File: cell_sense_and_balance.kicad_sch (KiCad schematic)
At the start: 40 parts, among them U1 BQ79616PAPRQ1

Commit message: SCH:[Hiarchy, Temp, Power]:Inital schmatics of temp, balance, power mostly there need to add design notes and layout notes.
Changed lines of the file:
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@@
-		)
-	)
-	(label "TAP[0..8]"
-		(at 116.84 53.34 0)
-		(fields_autoplaced yes)
-		(effects
-			(font
-				(size 1.27 1.27)
-			)
-			(justify left bottom)
-		)
-		(property "Netclass" "TAP"
-			(at 116.84 54.61 0)
-			(show_name no)
-			(do_not_autoplace no)
-			(effects
-				(font
-					(size 1.27 1.27)
-					(italic yes)
-				)
-				(justify left)
-			)
 		)
 	)
@@
 		)
 	)
-	(hierarchical_label "CELL_TAPS"
+	(hierarchical_label "TAP[0..8]"
 		(shape bidirectional)
 		(at 116.84 53.34 180)
@@
 			(justify right)
 		)
+		(property "Netclass" "TAP"
+			(at 106.68 55.88 0)
+			(show_name no)
+			(do_not_autoplace no)
+			(effects
+				(font
+					(size 1.27 1.27)
+					(italic yes)
+				)
+				(justify left)
+			)
+		)
 	)

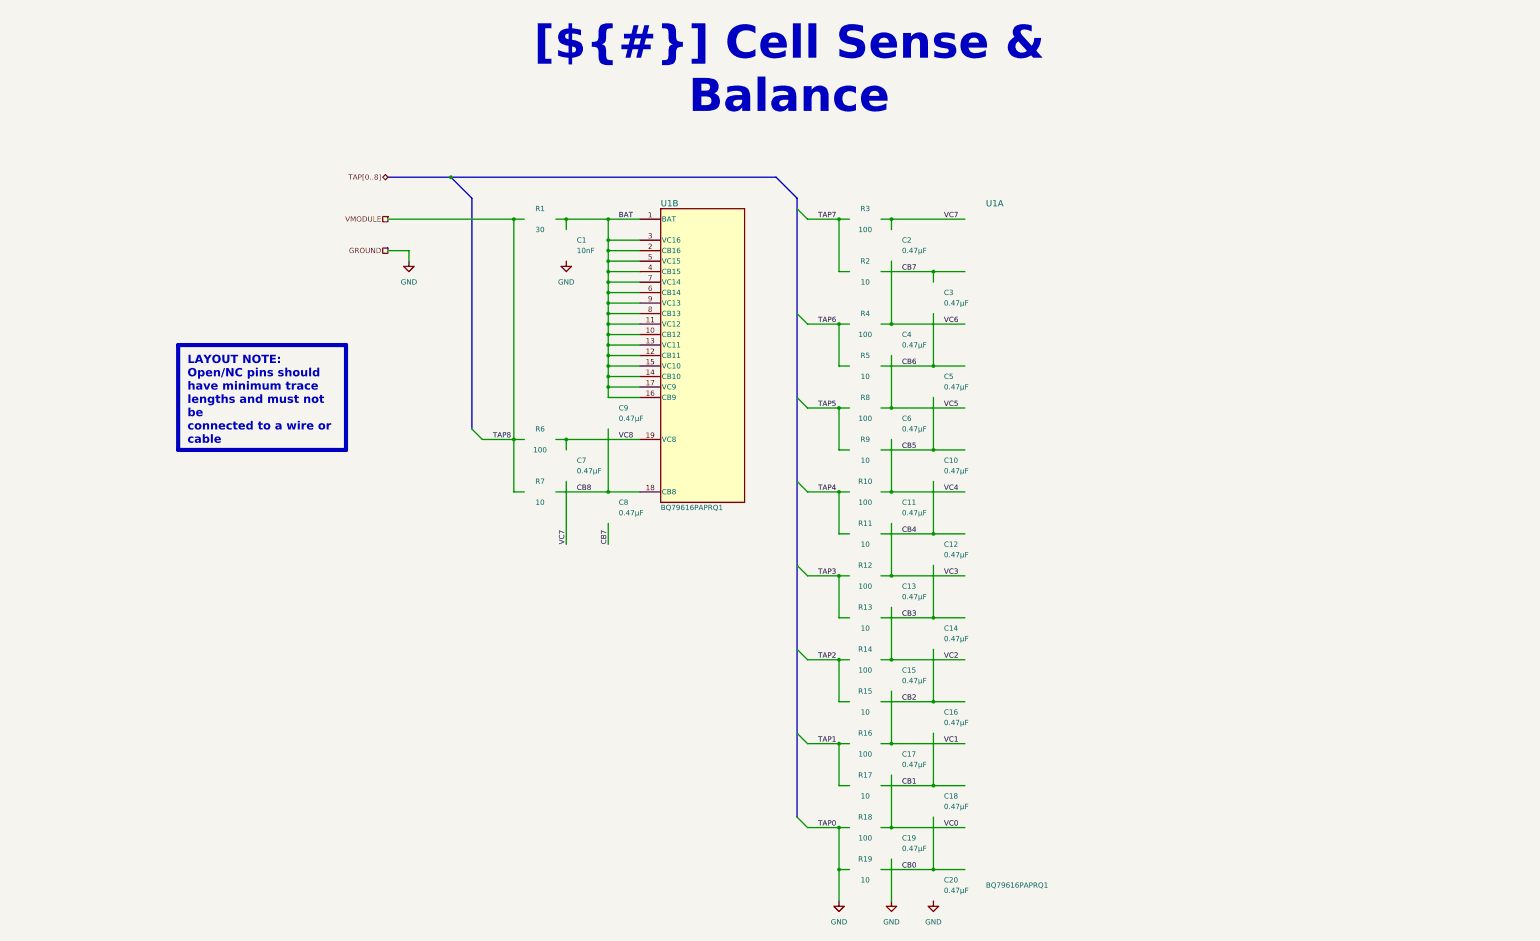
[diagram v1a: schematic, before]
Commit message: SCH: Schmatic is close to final, need to resolve a few ERC errors nothing major. Largest change will be adding seporate wires for VBAT and RefGround / Tap 0. connector position and types may change as mechaincal posision/layout is finalaized as well so holding off on layout for now.
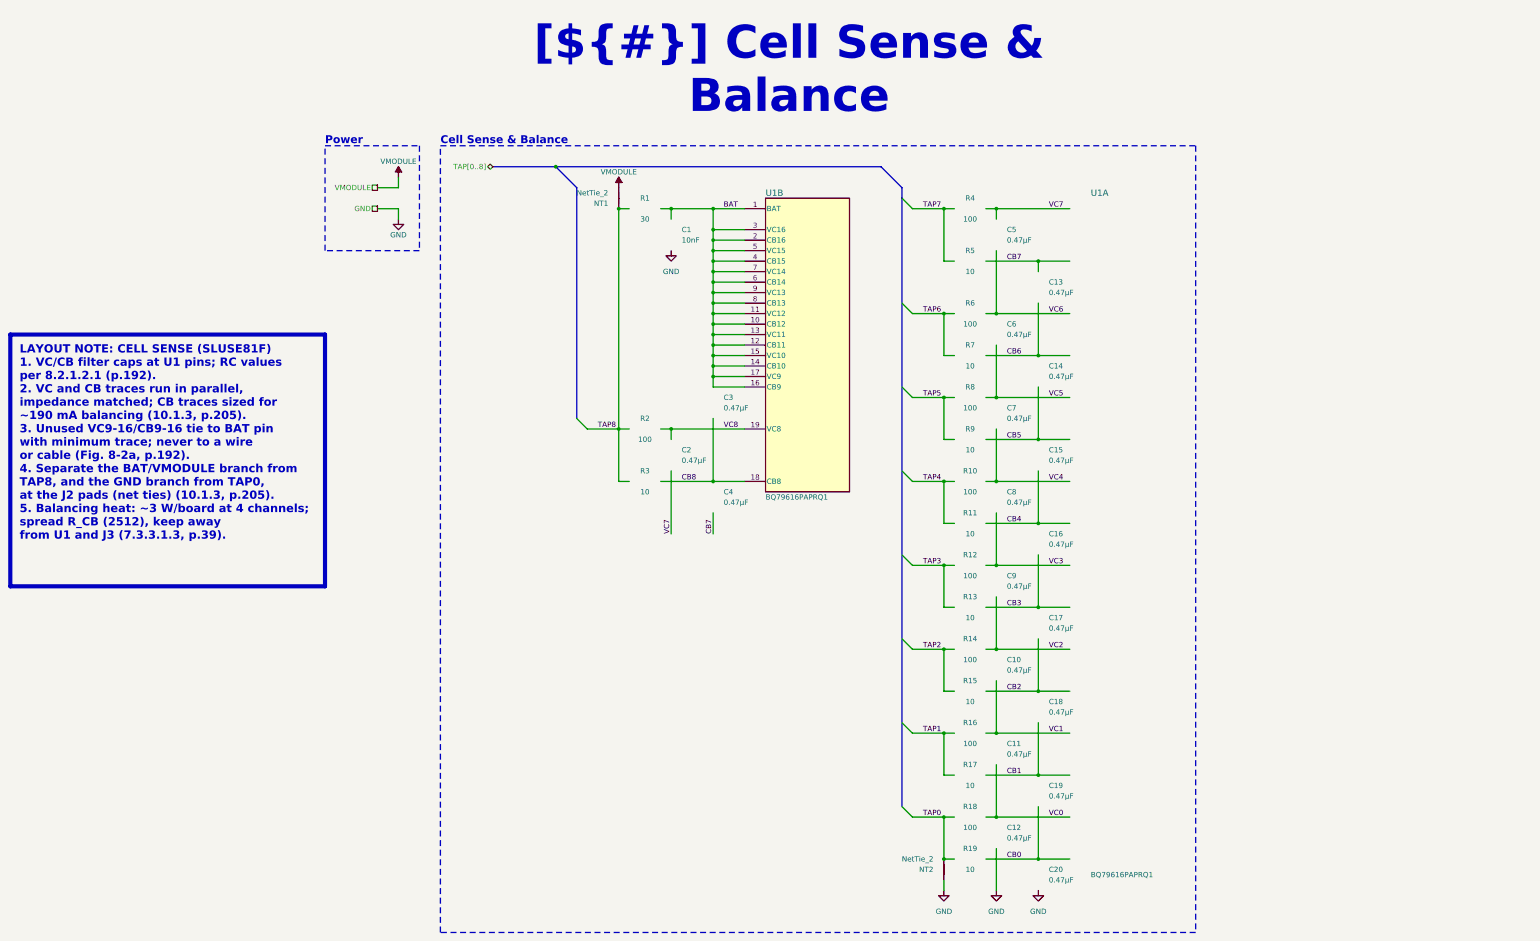
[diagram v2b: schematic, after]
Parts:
- added NT1, NT2: NetTie_2, symbol Device:NetTie_2
- renumbered C15 to C10, C17 to C11, C19 to C12, C3 to C13, C5 to C14, C10 to C15, C12 to C16, C14 to C17, C16 to C18, C18 to C19, C7 to C2, C9 to C3, C8 to C4, C2 to C5, C4 to C6, C6 to C7, C11 to C8, C13 to C9, R6 to R2, R7 to R3, R3 to R4, R2 to R5, R4 to R6, R5 to R7
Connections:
- net GND: now also NT2.1; no longer R18.1, R19.1
- net VMODULE: now also NT1.2; no longer R1.1, R2.1, R3.1
- new net TAP0: NT2.2, R18.1, R19.1
- new net TAP8: NT1.1, R1.1, R2.1, R3.1
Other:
- note added: "Cell Sense & Balance"
- note added: "Power"
- moved on the sheet: U1B

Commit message: SCH[Cleaning]:Updated Connectors not sure still, added sprate bat and ground connections, updated commincation conncetors. PCB[Layout]:Inital layout of compents need to fit on board size once tap connecton method is decided.
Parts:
- removed NT1, NT2: NetTie_2, symbol Device:NetTie_2
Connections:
- net TAP8: no longer R1.1
- net VMODULE: now also R1.1

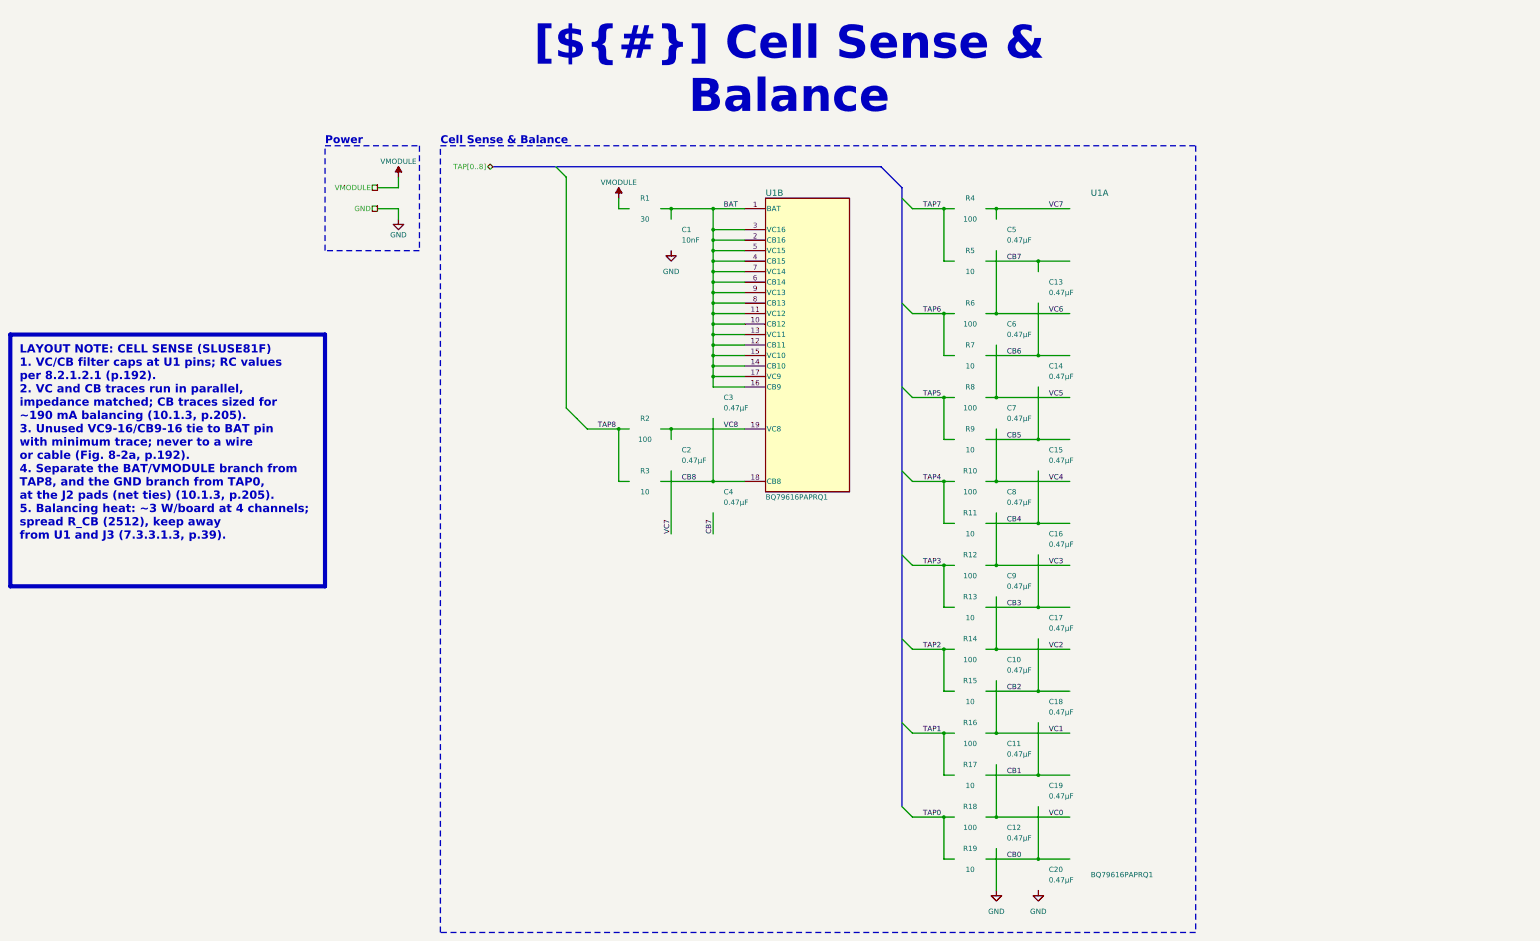
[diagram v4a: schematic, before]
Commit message: PCB[Test Points, Mechanical, Silk]: Finalized Mounting Points, Added Testpoints with adjecent silkscreen labels. SCH[Test Points, Notes]: Added/Updated notes for all pages, cleaned up errors spelling ect.
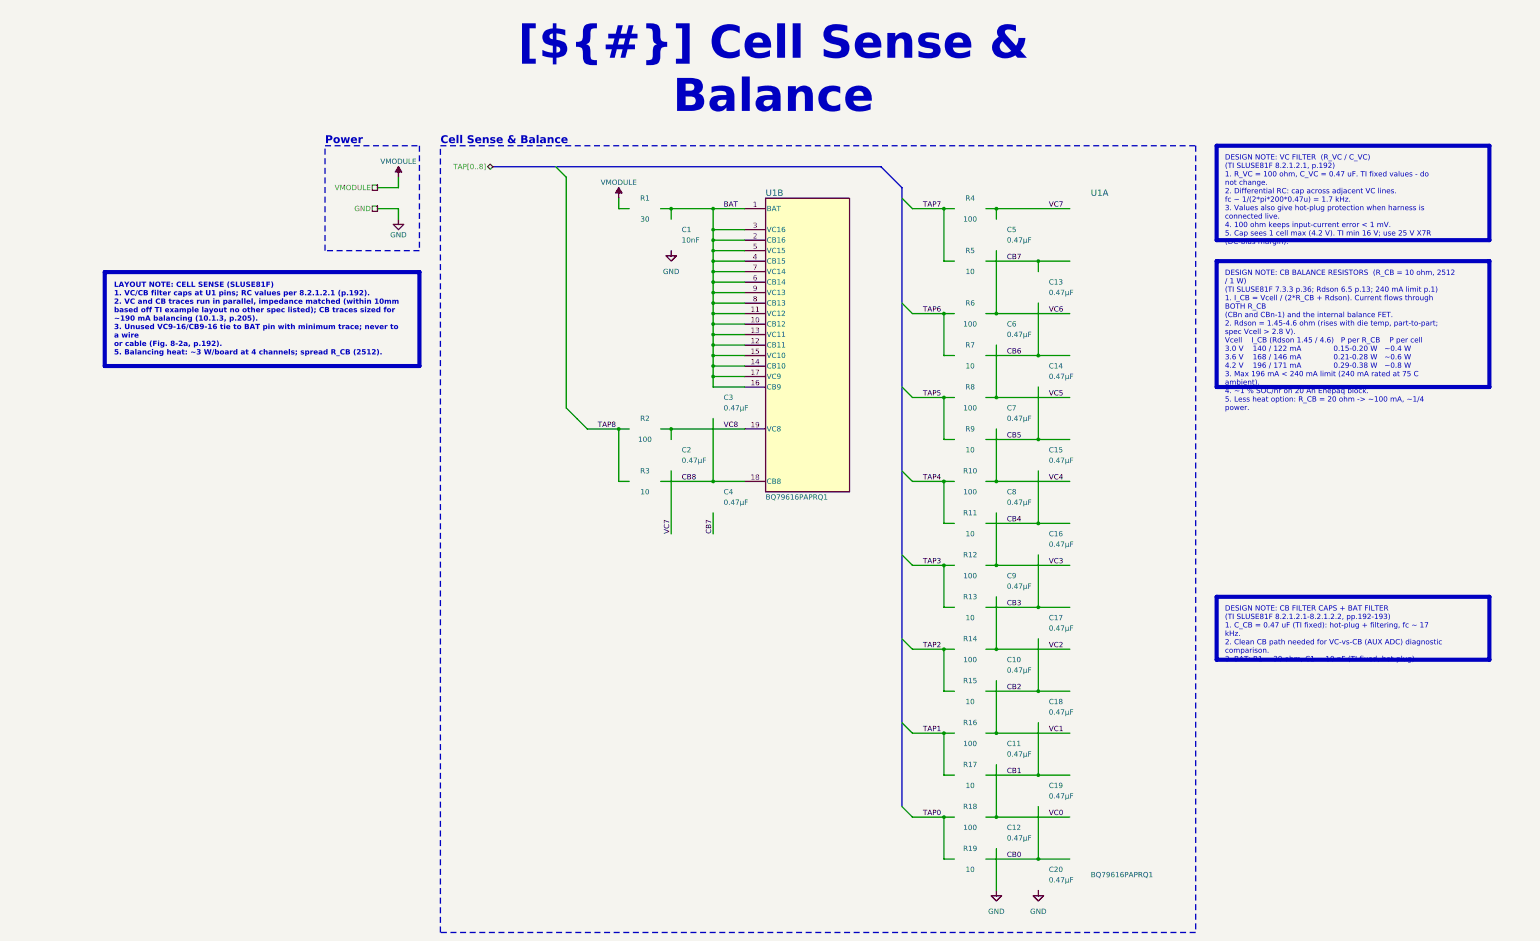
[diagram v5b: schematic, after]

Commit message: PCB[Trace Size, Testpad, Daisy]: Changed Bat Trace size FAT, Made test pads larger, small trace movement to clean up, daisy trace change. SCH[Notes]: Small notes changes.
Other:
- company: (none) -> ${COMPANY}
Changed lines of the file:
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@@
 	(title_block
 		(title "Cell Sense & Balance")
+		(date "2026-10-28")
+		(rev "${REVISION}")
+		(company "${COMPANY}")
 	)
 	(rectangle
@@
 		)
 	)
-	(text_box "DESIGN NOTE: VC FILTER  (R_VC / C_VC)\n(TI SLUSE81F 8.2.1.2.1, p.192)\n1. R_VC = 100 ohm, C_VC = 0.47 uF. TI fixed values - do not change.\n2. Differential RC: cap across adjacent VC lines.\n   fc ~ 1/(2*pi*200*0.47u) = 1.7 kHz.\n3. Values also give hot-plug protection when harness is connected live.\n4. 100 ohm keeps input-current error < 1 mV.\n5. Cap sees 1 cell max (4.2 V). TI min 16 V; use 25 V X7R (DC-bias margin)."
+	(text_box "DESIGN NOTE: VC FILTER  (R_VC / C_VC)\n(TI Datasheet 8.2.1.2.1, p.192)\n1. R_VC = 100 ohm, C_VC = 0.47 uF. TI fixed values, do not change.\n2. Differential RC: cap across adjacent VC lines.\n   fc ~ 1/(2*pi*200*0.47u) = 1.7 kHz.\n3. Values also give hot-plug protection when harness is connected live.\n4. 100 ohm keeps input-current error < 1 mV.\n5. Cap sees 1 cell max (4.2 V). TI min 16 V; use 25 V X7R (DC-bias margin)."
 		(exclude_from_sim no)
 		(at 317.5 45.72 0)
@@
 		)
 	)
-	(text_box "DESIGN NOTE: CB FILTER CAPS + BAT FILTER\n(TI SLUSE81F 8.2.1.2.1-8.2.1.2.2, pp.192-193)\n1. C_CB = 0.47 uF (TI fixed): hot-plug + filtering, fc ~ 17 kHz.\n2. Clean CB path needed for VC-vs-CB (AUX ADC) diagnostic comparison.\n3. BAT: R1 = 30 ohm, C1 = 10 nF (TI fixed, hot-plug)."
+	(text_box "DESIGN NOTE: CB FILTER CAPS + BAT FILTER\n(TI Datasheet 8.2.1.2.1-8.2.1.2.2, pp.192-193)\n1. C_CB = 0.47 uF (TI fixed): hot-plug + filtering, fc ~ 17 kHz.\n2. Clean CB path needed for VC-vs-CB (AUX ADC) diagnostic comparison.\n3. BAT: R1 = 30 ohm, C1 = 10 nF (TI fixed, hot-plug)."
 		(exclude_from_sim no)
 		(at 317.5 154.94 0)
@@
 		)
 	)
-	(text_box "DESIGN NOTE: CB BALANCE RESISTORS  (R_CB = 10 ohm, 2512 / 1 W)\n(TI SLUSE81F 7.3.3 p.36; Rdson 6.5 p.13; 240 mA limit p.1)\n1. I_CB = Vcell / (2*R_CB + Rdson). Current flows through BOTH R_CB\n   (CBn and CBn-1) and the internal balance FET.\n2. Rdson = 1.45-4.6 ohm (rises with die temp, part-to-part; spec Vcell > 2.8 V).\n   Vcell    I_CB (Rdson 1.45 / 4.6)   P per R_CB    P per cell\n   3.0 V    140 / 122 mA              0.15-0.20 W   ~0.4 W\n   3.6 V    168 / 146 mA              0.21-0.28 W   ~0.6 W\n   4.2 V    196 / 171 mA              0.29-0.38 W   ~0.8 W\n3. Max 196 mA < 240 mA limit (240 mA rated at 75 C ambient).\n4. ~1 % SOC/hr on 20 Ah Enepaq block.\n5. Less heat option: R_CB = 20 ohm -> ~100 mA, ~1/4 power."
+	(text_box "DESIGN NOTE: CB BALANCE RESISTORS  (R_CB = 10 ohm, 2512 / 1 W)\n(TI Datasheet 7.3.3 p.36; Rdson 6.5 p.13; 240 mA limit p.1)\n1. I_CB = Vcell / (2*R_CB + Rdson). Current flows through BOTH R_CB\n   (CBn and CBn-1) and the internal balance FET.\n2. Rdson = 1.45-4.6 ohm (rises with die temp, part-to-part; spec Vcell > 2.8 V).\n   Vcell    I_CB (Rdson 1.45 / 4.6)   P per R_CB    P per cell\n   3.0 V    140 / 122 mA              0.15-0.20 W   ~0.4 W\n   3.6 V    168 / 146 mA              0.21-0.28 W   ~0.6 W\n   4.2 V    196 / 171 mA              0.29-0.38 W   ~0.8 W\n3. Max 196 mA < 240 mA limit (240 mA rated at 75 C ambient).\n4. ~1 % SOC/hr on 20 Ah Enepaq block.\n5. Less heat option: R_CB = 20 ohm -> ~100 mA, ~1/4 power."
 		(exclude_from_sim no)
 		(at 317.5 73.66 0)
